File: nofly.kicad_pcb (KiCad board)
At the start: 4 copper layers, 23.6 x 8.3 mm, 8 parts, among them J1 TYPE-C-31-M-12, J2 781710004 / M1201RS-04-BK, U1 USBLC6-2P6

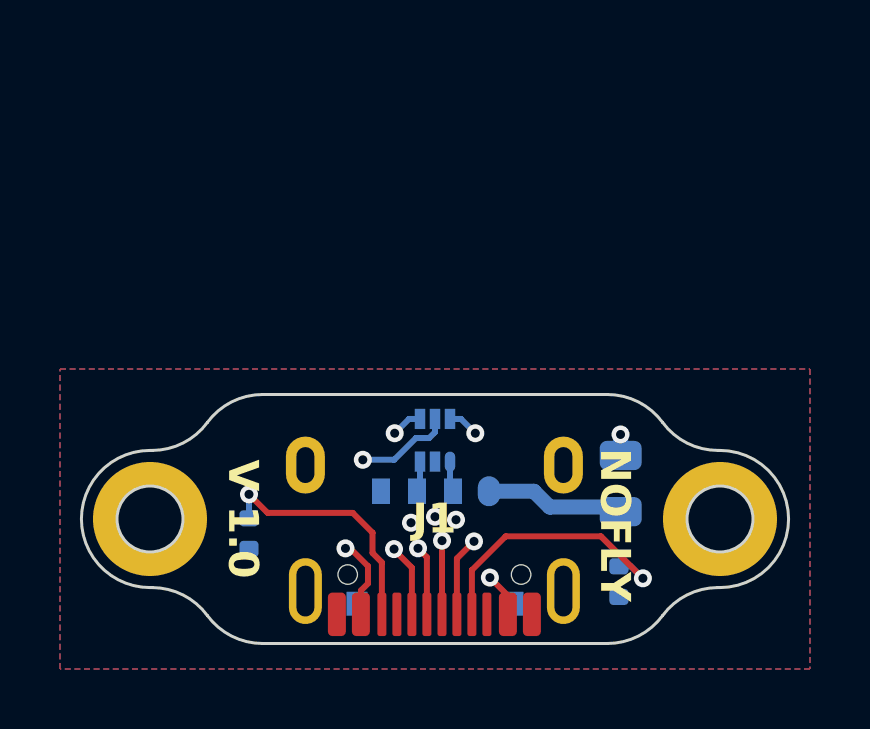
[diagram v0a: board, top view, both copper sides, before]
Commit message: Add pannelization
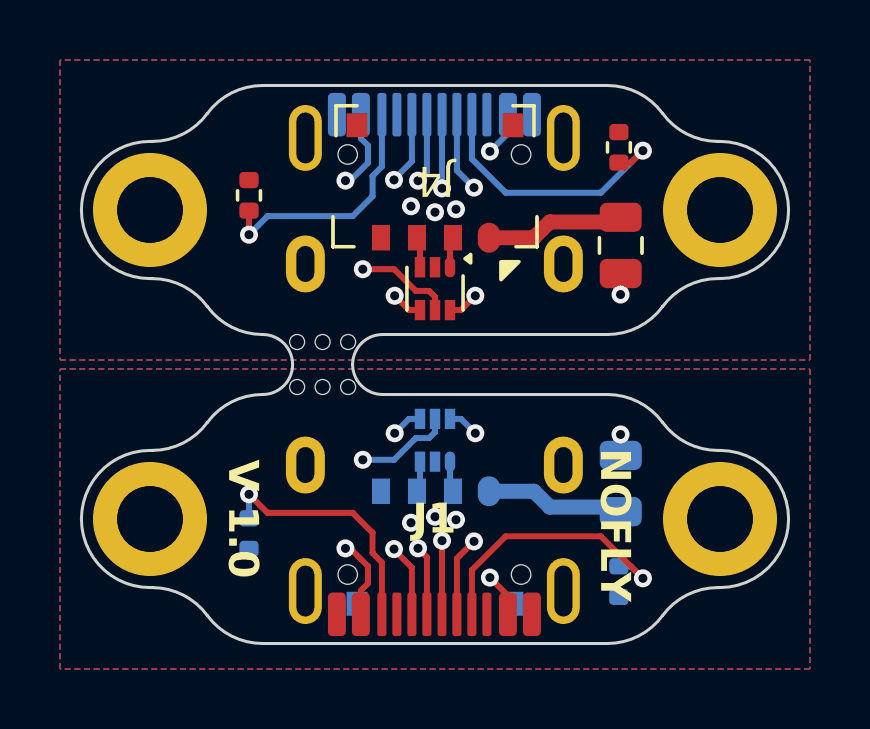
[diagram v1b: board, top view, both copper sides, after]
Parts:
- added B1: MouseBite, Panelization:MouseBite-Part_2.0x2.0mm_outset_D0.5mm_P0.85mm_3h, F.Cu at (131.6, 61.2)
- added B2: MouseBite, Panelization:MouseBite-Part_2.0x2.0mm_outset_D0.5mm_P0.85mm_3h, F.Cu at (131.6, 63.2)
- added F2: SMD0805-050, Fuse:Fuse_0805_2012Metric, F.Cu at (141.5, 58.3)
- added H1: Mount, MountingHole:MountingHole_2.2mm_M2_DIN965_Pad, B.Cu at (125.8, 57.1)
- added H2: Mount, MountingHole:MountingHole_2.2mm_M2_DIN965_Pad, B.Cu at (144.8, 57.1)
- added J3: TYPE-C-31-M-12, acheron_Connectors:USB_C_Receptacle_Hroparts_TYPE-C-31-M-12, B.Cu at (135.3, 53.2)
- added J4: 781710004 / M1201RS-04-BK, acheron_Connectors:MOLEX_PicoEZMate_781710004, F.Cu at (135.3, 58.0)
- added R3: 5.1k, Resistor_SMD:R_0402_1005Metric, F.Cu at (141.4, 55.0)
- added R4: 5.1k, Resistor_SMD:R_0402_1005Metric, F.Cu at (129.1, 56.6)
- added U2: USBLC6-2P6, Package_TO_SOT_SMD:SOT-563, F.Cu at (135.3, 59.7)
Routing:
- net VBUS: track 31.0 -> 62.0 mm, vias 4 -> 8
- net D+: track 16.4 -> 32.9 mm, vias 3 -> 6
- net D-: track 12.1 -> 24.2 mm, vias 3 -> 6
- net Net-(J1-CC1): track 9.19 -> 18.4 mm, vias 1 -> 2
- net Net-(J1-CC2): track 8.30 -> 16.6 mm, vias 1 -> 2
- net 5V: track 4.67 -> 9.34 mm
- net DO+: track 1.41 -> 2.83 mm
- net DO-: track 1.36 -> 2.71 mm
- net GND: vias 3 -> 6
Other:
- board size 23.6 x 8.3 mm -> 23.6 x 18.6 mm
